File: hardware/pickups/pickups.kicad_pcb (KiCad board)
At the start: 2 copper layers, 40.5 x 45 mm, 6 parts

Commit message: Update pickups pcb
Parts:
- removed Out: Out, moonbeaminteractive:pickup_contact
- removed REF**: VCC, pickup_contact_bottom_right
- removed REF**: GND, moonbeaminteractive:pickup_contact_bottom_left
- added P1: VCC, pickup_contact_bottom_left, F.Cu at (97.5, 95.5)
- added P2: OUT, pickup_contact, F.Cu at (107.8, 87.0)
- added P3: GND, pickup_contact_bottom_right, F.Cu at (118.0, 95.5)
- moved R2 22.1 mm to (118.0, 80.5), turned to 270 degrees
- moved R1 16.7 mm to (97.5, 80.5)
- moved R3 11.9 mm to (107.8, 71.5), turned to 90 degrees
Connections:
- R1 pad 2: GND -> Net-(P1-Pad1)
- R2 pad 2: VCC -> Net-(P3-Pad1)
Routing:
- net Net-(P3-Pad1): track 0.00 -> 8.75 mm
- net Net-(P1-Pad1): track 0.00 -> 8.75 mm
- net Net-(R1-Pad1): track 35.0 -> 43.1 mm
- net Net-(P2-Pad1): track 12.5 -> 6.25 mm
- net VCC: track 6.00 -> 0.00 mm
- net GND: track 5.50 -> 0.00 mm
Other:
- board size 40.5 x 45 mm -> 40.5 x 45.6 mm
- net class Default: clearance 0.2 -> 0.8; trace_width 0.25 -> 1
- net class Pickup added: clearance 0.8, trace_width 1, via_dia 0.6, via_drill 0.4
- rule trace_clearance: 0.2 -> 0.8

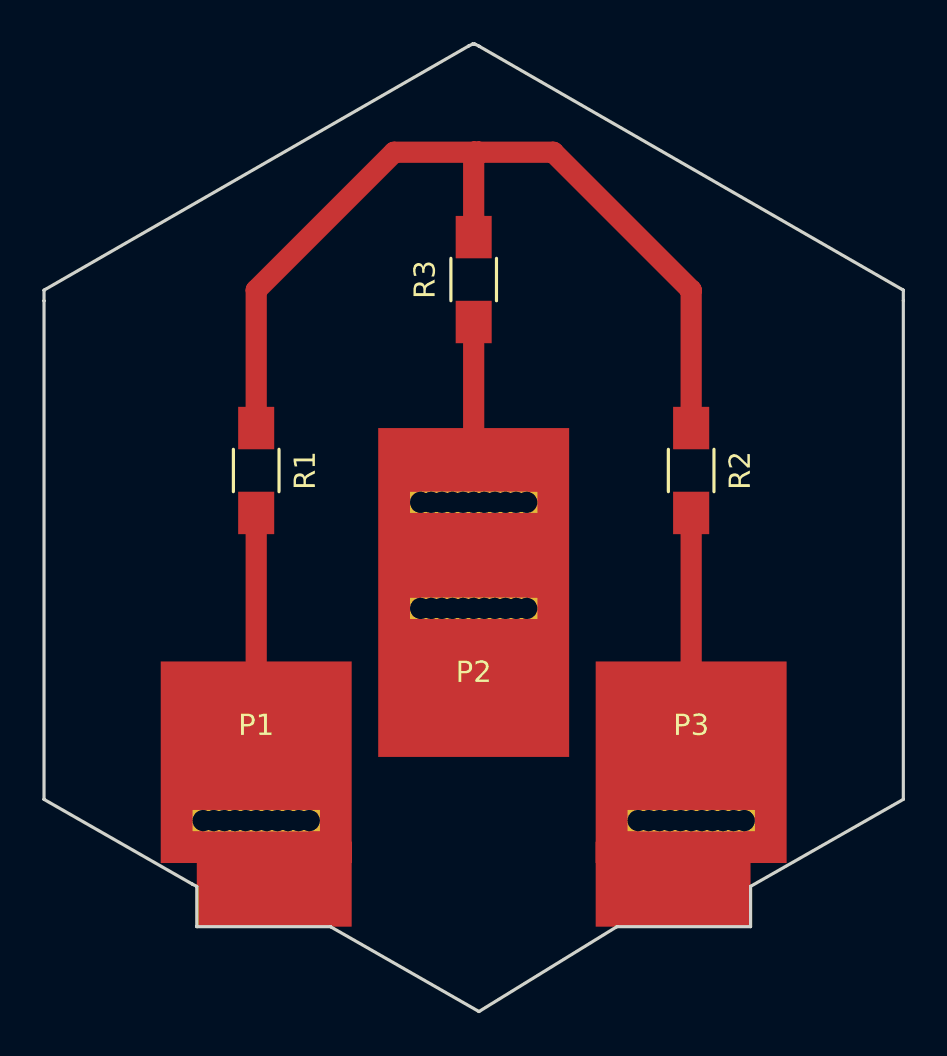
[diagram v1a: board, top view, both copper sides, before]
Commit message: changed resistor footprints to universal type
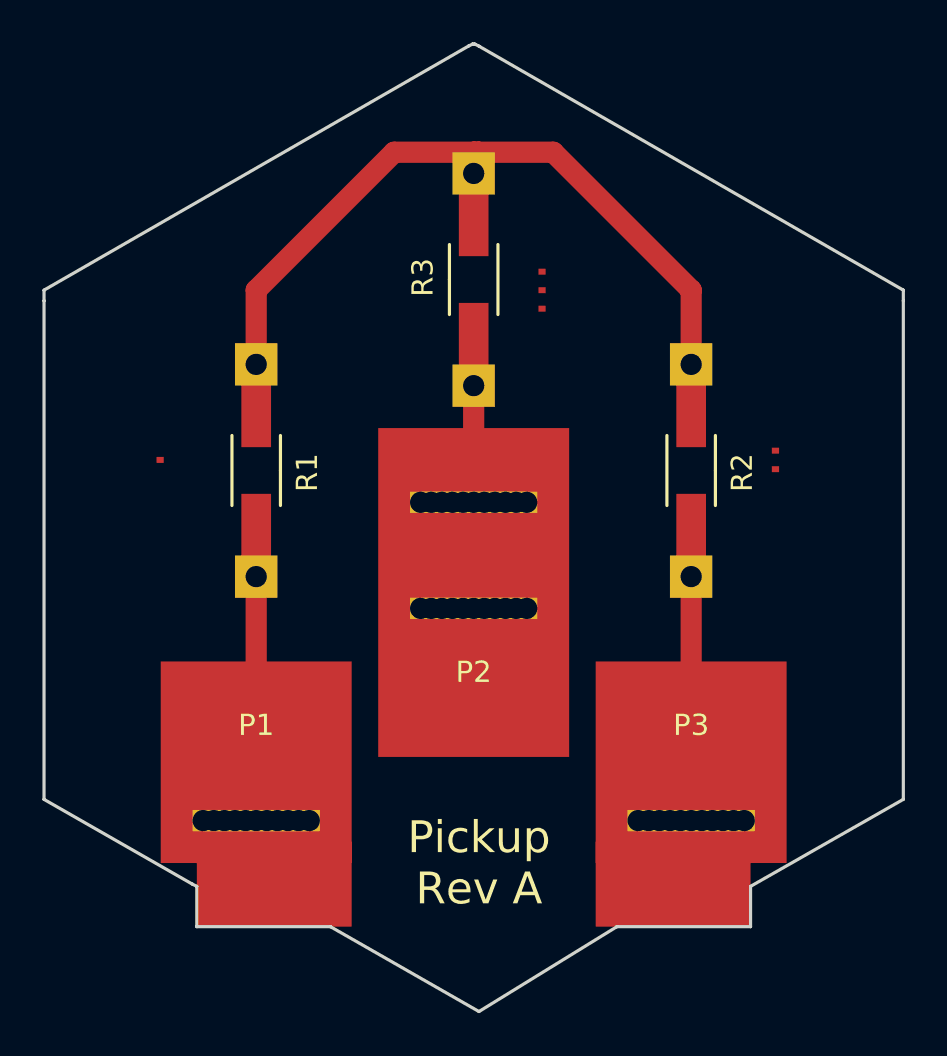
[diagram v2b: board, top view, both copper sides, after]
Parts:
- R1, R2, R3: footprint Resistors_SMD:R_1206_HandSoldering -> Resistors_Universal:Resistor_SMD+THTuniversal_1206_RM10_HandSoldering
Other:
- board text added: "Pickup Rev A"
- board text added: "·"
- board text added: "··"
- board text added: "···"
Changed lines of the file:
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@@
-(kicad_pcb (version 4) (host pcbnew 4.0.4-stable)
+(kicad_pcb (version 4) (host pcbnew 4.0.1-stable)
   (general
-    (links 16)
-    (no_connects 0)
-    (area 87.424999 60.924999 128.075001 106.075001)
+    (links 22)
+    (no_connects 5)
+    (area 87.424999 60.324999 128.075001 106.075001)
     (thickness 1.6)
-    (drawings 18)
+    (drawings 22)
     (tracks 11)
     (zones 0)
@@
   )
   (page A4)
+  (title_block
+    (title Pickup)
+    (date 2016-12-13)
+    (rev A)
+    (company "Moonbeam Interactive")
+    (comment 1 "Diego Alvarez")
+    (comment 2 "Matthew Swarts")
+  )
   (layers
     (0 F.Cu signal)
@@
     (pad_to_mask_clearance 0.2)
     (aux_axis_origin 0 0)
-    (visible_elements FFFFFF7F)
+    (visible_elements 7FFFFFFF)
     (pcbplotparams
       (layerselection 0x01000_00000001)
@@
       (net 4 "Net-(P3-Pad1)"))
   )
-  (module Resistors_SMD:R_1206_HandSoldering (layer F.Cu)
+  (module Resistors_Universal:Resistor_SMD+THTuniversal_1206_RM10_HandSoldering (layer F.Cu)
+    (at 107.75 71.5 90)
+    (descr "Resistor, SMD+THT, universal, 1206, RM10, HandSoldering,")
+    (tags "Resistor, SMD+THT, universal, 1206, RM10, Hand soldering,")
+    (fp_text reference R3 (at 0.09906 -2.4003 90) (layer F.SilkS)
+      (effects (font (size 1 1) (thickness 0.15)))
+    )
+    (fp_text value R (at 2.70002 2.70002 90) (layer F.Fab)
+      (effects (font (size 1 1) (thickness 0.15)))
+    )
+    (fp_line (start 1.651 1.143) (end -1.651 1.143) (layer F.SilkS) (width 0.15))
+    (fp_line (start 0 -1.143) (end -1.651 -1.143) (layer F.SilkS) (width 0.15))
+    (fp_line (start 0 -1.143) (end 1.651 -1.143) (layer F.SilkS) (width 0.15))
+    (pad 1 smd rect (at -2.60096 0 90) (size 2.99974 1.39954) (layers F.Cu F.Paste F.Mask)
+      (net 3 "Net-(P2-Pad1)"))
+    (pad 2 smd rect (at 2.60096 0 90) (size 2.99974 1.39954) (layers F.Cu F.Paste F.Mask)
+      (net 1 "Net-(R1-Pad1)"))
+    (pad 1 thru_hole rect (at -5.00126 0 90) (size 1.99898 1.99898) (drill 1.00076) (layers *.Cu *.Mask F.SilkS)
+      (net 3 "Net-(P2-Pad1)"))
+    (pad 2 thru_hole rect (at 5.00126 0 90) (size 1.99898 1.99898) (drill 1.00076) (layers *.Cu *.Mask F.SilkS)
+      (net 1 "Net-(R1-Pad1)"))
+  )
+  (module Resistors_Universal:Resistor_SMD+THTuniversal_1206_RM10_HandSoldering (layer F.Cu)
+    (at 118 80.5 270)
+    (descr "Resistor, SMD+THT, universal, 1206, RM10, HandSoldering,")
+    (tags "Resistor, SMD+THT, universal, 1206, RM10, Hand soldering,")
+    (fp_text reference R2 (at 0.09906 -2.4003 270) (layer F.SilkS)
+      (effects (font (size 1 1) (thickness 0.15)))
+    )
+    (fp_text value R (at 2.70002 2.70002 270) (layer F.Fab)
+      (effects (font (size 1 1) (thickness 0.15)))
+    )
+    (fp_line (start 1.651 1.143) (end -1.651 1.143) (layer F.SilkS) (width 0.15))
+    (fp_line (start 0 -1.143) (end -1.651 -1.143) (layer F.SilkS) (width 0.15))
+    (fp_line (start 0 -1.143) (end 1.651 -1.143) (layer F.SilkS) (width 0.15))
+    (pad 1 smd rect (at -2.60096 0 270) (size 2.99974 1.39954) (layers F.Cu F.Paste F.Mask)
+      (net 1 "Net-(R1-Pad1)"))
+    (pad 2 smd rect (at 2.60096 0 270) (size 2.99974 1.39954) (layers F.Cu F.Paste F.Mask)
+      (net 4 "Net-(P3-Pad1)"))
+    (pad 1 thru_hole rect (at -5.00126 0 270) (size 1.99898 1.99898) (drill 1.00076) (layers *.Cu *.Mask F.SilkS)
+      (net 1 "Net-(R1-Pad1)"))
+    (pad 2 thru_hole rect (at 5.00126 0 270) (size 1.99898 1.99898) (drill 1.00076) (layers *.Cu *.Mask F.SilkS)
+      (net 4 "Net-(P3-Pad1)"))
+  )
+  (module Resistors_Universal:Resistor_SMD+THTuniversal_1206_RM10_HandSoldering (layer F.Cu)
     (at 97.5 80.5 270)
-    (descr "Resistor SMD 1206, hand soldering")
-    (tags "resistor 1206")
-    (attr smd)
-    (fp_text reference R1 (at 0 -2.3 270) (layer F.SilkS)
-      (effects (font (size 1 1) (thickness 0.15)))
-    )
-    (fp_text value R (at 0 2.3 270) (layer F.Fab)
-      (effects (font (size 1 1) (thickness 0.15)))
-    )
-    (fp_line (start -1.6 0.8) (end -1.6 -0.8) (layer F.Fab) (width 0.1))
-    (fp_line (start 1.6 0.8) (end -1.6 0.8) (layer F.Fab) (width 0.1))
-    (fp_line (start 1.6 -0.8) (end 1.6 0.8) (layer F.Fab) (width 0.1))
-    (fp_line (start -1.6 -0.8) (end 1.6 -0.8) (layer F.Fab) (width 0.1))
-    (fp_line (start -3.3 -1.2) (end 3.3 -1.2) (layer F.CrtYd) (width 0.05))
-    (fp_line (start -3.3 1.2) (end 3.3 1.2) (layer F.CrtYd) (width 0.05))
-    (fp_line (start -3.3 -1.2) (end -3.3 1.2) (layer F.CrtYd) (width 0.05))
-    (fp_line (start 3.3 -1.2) (end 3.3 1.2) (layer F.CrtYd) (width 0.05))
-    (fp_line (start 1 1.075) (end -1 1.075) (layer F.SilkS) (width 0.15))
-    (fp_line (start -1 -1.075) (end 1 -1.075) (layer F.SilkS) (width 0.15))
-    (pad 1 smd rect (at -2 0 270) (size 2 1.7) (layers F.Cu F.Paste F.Mask)
-      (net 1 "Net-(R1-Pad1)"))
-    (pad 2 smd rect (at 2 0 270) (size 2 1.7) (layers F.Cu F.Paste F.Mask)
+    (descr "Resistor, SMD+THT, universal, 1206, RM10, HandSoldering,")
+    (tags "Resistor, SMD+THT, universal, 1206, RM10, Hand soldering,")
+    (fp_text reference R1 (at 0.09906 -2.4003 270) (layer F.SilkS)
+      (effects (font (size 1 1) (thickness 0.15)))
+    )
+    (fp_text value R (at 2.70002 2.70002 270) (layer F.Fab)
+      (effects (font (size 1 1) (thickness 0.15)))
+    )
+    (fp_line (start 1.651 1.143) (end -1.651 1.143) (layer F.SilkS) (width 0.15))
+    (fp_line (start 0 -1.143) (end -1.651 -1.143) (layer F.SilkS) (width 0.15))
+    (fp_line (start 0 -1.143) (end 1.651 -1.143) (layer F.SilkS) (width 0.15))
+    (pad 1 smd rect (at -2.60096 0 270) (size 2.99974 1.39954) (layers F.Cu F.Paste F.Mask)
+      (net 1 "Net-(R1-Pad1)"))
+    (pad 2 smd rect (at 2.60096 0 270) (size 2.99974 1.39954) (layers F.Cu F.Paste F.Mask)
       (net 2 "Net-(P1-Pad1)"))
-    (model Resistors_SMD.3dshapes/R_1206_HandSoldering.wrl
-      (at (xyz 0 0 0))
-      (scale (xyz 1 1 1))
-      (rotate (xyz 0 0 0))
-    )
-  )
-  (module Resistors_SMD:R_1206_HandSoldering (layer F.Cu)
-    (at 118 80.5 270)
-    (descr "Resistor SMD 1206, hand soldering")
-    (tags "resistor 1206")
-    (attr smd)
-    (fp_text reference R2 (at 0 -2.3 270) (layer F.SilkS)
-      (effects (font (size 1 1) (thickness 0.15)))
-    )
-    (fp_text value R (at 0 2.3 270) (layer F.Fab)
-      (effects (font (size 1 1) (thickness 0.15)))
-    )
-    (fp_line (start -1.6 0.8) (end -1.6 -0.8) (layer F.Fab) (width 0.1))
-    (fp_line (start 1.6 0.8) (end -1.6 0.8) (layer F.Fab) (width 0.1))
-    (fp_line (start 1.6 -0.8) (end 1.6 0.8) (layer F.Fab) (width 0.1))
-    (fp_line (start -1.6 -0.8) (end 1.6 -0.8) (layer F.Fab) (width 0.1))
-    (fp_line (start -3.3 -1.2) (end 3.3 -1.2) (layer F.CrtYd) (width 0.05))
-    (fp_line (start -3.3 1.2) (end 3.3 1.2) (layer F.CrtYd) (width 0.05))
-    (fp_line (start -3.3 -1.2) (end -3.3 1.2) (layer F.CrtYd) (width 0.05))
-    (fp_line (start 3.3 -1.2) (end 3.3 1.2) (layer F.CrtYd) (width 0.05))
-    (fp_line (start 1 1.075) (end -1 1.075) (layer F.SilkS) (width 0.15))
-    (fp_line (start -1 -1.075) (end 1 -1.075) (layer F.SilkS) (width 0.15))
-    (pad 1 smd rect (at -2 0 270) (size 2 1.7) (layers F.Cu F.Paste F.Mask)
-      (net 1 "Net-(R1-Pad1)"))
-    (pad 2 smd rect (at 2 0 270) (size 2 1.7) (layers F.Cu F.Paste F.Mask)
-      (net 4 "Net-(P3-Pad1)"))
-    (model Resistors_SMD.3dshapes/R_1206_HandSoldering.wrl
-      (at (xyz 0 0 0))
-      (scale (xyz 1 1 1))
-      (rotate (xyz 0 0 0))
-    )
-  )
-  (module Resistors_SMD:R_1206_HandSoldering (layer F.Cu)
-    (at 107.75 71.5 90)
-    (descr "Resistor SMD 1206, hand soldering")
-    (tags "resistor 1206")
-    (attr smd)
-    (fp_text reference R3 (at 0 -2.3 90) (layer F.SilkS)
-      (effects (font (size 1 1) (thickness 0.15)))
-    )
-    (fp_text value R (at 0 2.3 90) (layer F.Fab)
-      (effects (font (size 1 1) (thickness 0.15)))
-    )
-    (fp_line (start -1.6 0.8) (end -1.6 -0.8) (layer F.Fab) (width 0.1))
-    (fp_line (start 1.6 0.8) (end -1.6 0.8) (layer F.Fab) (width 0.1))
-    (fp_line (start 1.6 -0.8) (end 1.6 0.8) (layer F.Fab) (width 0.1))
-    (fp_line (start -1.6 -0.8) (end 1.6 -0.8) (layer F.Fab) (width 0.1))
-    (fp_line (start -3.3 -1.2) (end 3.3 -1.2) (layer F.CrtYd) (width 0.05))
-    (fp_line (start -3.3 1.2) (end 3.3 1.2) (layer F.CrtYd) (width 0.05))
-    (fp_line (start -3.3 -1.2) (end -3.3 1.2) (layer F.CrtYd) (width 0.05))
-    (fp_line (start 3.3 -1.2) (end 3.3 1.2) (layer F.CrtYd) (width 0.05))
-    (fp_line (start 1 1.075) (end -1 1.075) (layer F.SilkS) (width 0.15))
-    (fp_line (start -1 -1.075) (end 1 -1.075) (layer F.SilkS) (width 0.15))
-    (pad 1 smd rect (at -2 0 90) (size 2 1.7) (layers F.Cu F.Paste F.Mask)
-      (net 3 "Net-(P2-Pad1)"))
-    (pad 2 smd rect (at 2 0 90) (size 2 1.7) (layers F.Cu F.Paste F.Mask)
-      (net 1 "Net-(R1-Pad1)"))
-    (model Resistors_SMD.3dshapes/R_1206_HandSoldering.wrl
-      (at (xyz 0 0 0))
-      (scale (xyz 1 1 1))
-      (rotate (xyz 0 0 0))
-    )
+    (pad 1 thru_hole rect (at -5.00126 0 270) (size 1.99898 1.99898) (drill 1.00076) (layers *.Cu *.Mask F.SilkS)
+      (net 1 "Net-(R1-Pad1)"))
+    (pad 2 thru_hole rect (at 5.00126 0 270) (size 1.99898 1.99898) (drill 1.00076) (layers *.Cu *.Mask F.SilkS)
+      (net 2 "Net-(P1-Pad1)"))
+  )
+  (gr_text ·· (at 122 80 90) (layer F.Cu)
+    (effects (font (size 2 2) (thickness 0.2)))
+  )
+  (gr_text · (at 93 80 90) (layer F.Cu)
+    (effects (font (size 2 2) (thickness 0.2)))
+  )
+  (gr_text ··· (at 111 72 90) (layer F.Cu)
+    (effects (font (size 2 2) (thickness 0.2)))
+  )
+  (gr_text "Pickup\nRev A" (at 108 99) (layer F.SilkS)
+    (effects (font (size 1.5 1.5) (thickness 0.3)))
   )
   (gr_line (start 107.8 60.4) (end 108 60.5) (angle 90) (layer Edge.Cuts) (width 0.15))
